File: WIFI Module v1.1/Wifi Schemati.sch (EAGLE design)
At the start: 25 parts, among them IC1 PIC24FVXXKA302-SP

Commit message: Moving Around Board
- Rotated ESP 180, fixed reprog issue
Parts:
- added SHORT_TO_RST: (no value), pinhead:PINHD-1X1
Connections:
- removed net N$3: R3.2, U$1.GPIO2
- new net N$12: R4.1, R5.1
- net 3.3V: no longer R4.1, R5.2
- net CLK: now also R3.2
- net FLSH_MD: no longer R4.2
- net MOSI: now also R4.2
- net N$1: now also SHORT_TO_RST.1; no longer R5.1
- net SS: now also R5.2

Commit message: v1.1 PCB Changes
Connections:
- removed net N$12: R4.1, R5.1
- net 3.3V: no longer R3.1
- net VDD: now also R3.1, R4.1, R5.1
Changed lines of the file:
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@@
 <?xml version="1.0" encoding="utf-8"?>
 <!DOCTYPE eagle SYSTEM "eagle.dtd">
-<eagle version="9.2.2">
+<eagle version="9.3.0">
 <drawing>
 <settings>
@@
 <label x="0" y="88.9" size="1.778" layer="95"/>
 </segment>
+<segment>
+<pinref part="R5" gate="G$1" pin="1"/>
+<wire x1="25.4" y1="25.4" x2="27.94" y2="25.4" width="0.1524" layer="91"/>
+<wire x1="27.94" y1="22.86" x2="27.94" y2="25.4" width="0.1524" layer="91"/>
+<pinref part="R3" gate="G$1" pin="1"/>
+<wire x1="25.4" y1="22.86" x2="27.94" y2="22.86" width="0.1524" layer="91"/>
+<label x="27.94" y="22.86" size="1.778" layer="95"/>
+<pinref part="R4" gate="G$1" pin="1"/>
+<wire x1="25.4" y1="20.32" x2="27.94" y2="20.32" width="0.1524" layer="91"/>
+<wire x1="27.94" y1="20.32" x2="27.94" y2="22.86" width="0.1524" layer="91"/>
+<junction x="27.94" y="22.86"/>
+</segment>
 </net>
 <net name="SPI_LIGHT" class="0">
@@
 <wire x1="243.84" y1="20.32" x2="238.76" y2="20.32" width="0.1524" layer="91"/>
 </segment>
-<segment>
-<pinref part="R3" gate="G$1" pin="1"/>
-<wire x1="25.4" y1="22.86" x2="30.48" y2="22.86" width="0.1524" layer="91"/>
-<label x="30.48" y="22.86" size="1.778" layer="95"/>
-</segment>
 </net>
 <net name="N$2" class="0">
@@
 </segment>
 </net>
-<net name="N$12" class="0">
-<segment>
-<pinref part="R5" gate="G$1" pin="1"/>
-<wire x1="25.4" y1="25.4" x2="27.94" y2="25.4" width="0.1524" layer="91"/>
-<pinref part="R4" gate="G$1" pin="1"/>
-<wire x1="25.4" y1="20.32" x2="27.94" y2="20.32" width="0.1524" layer="91"/>
-<wire x1="27.94" y1="20.32" x2="27.94" y2="25.4" width="0.1524" layer="91"/>
-</segment>
-</net>

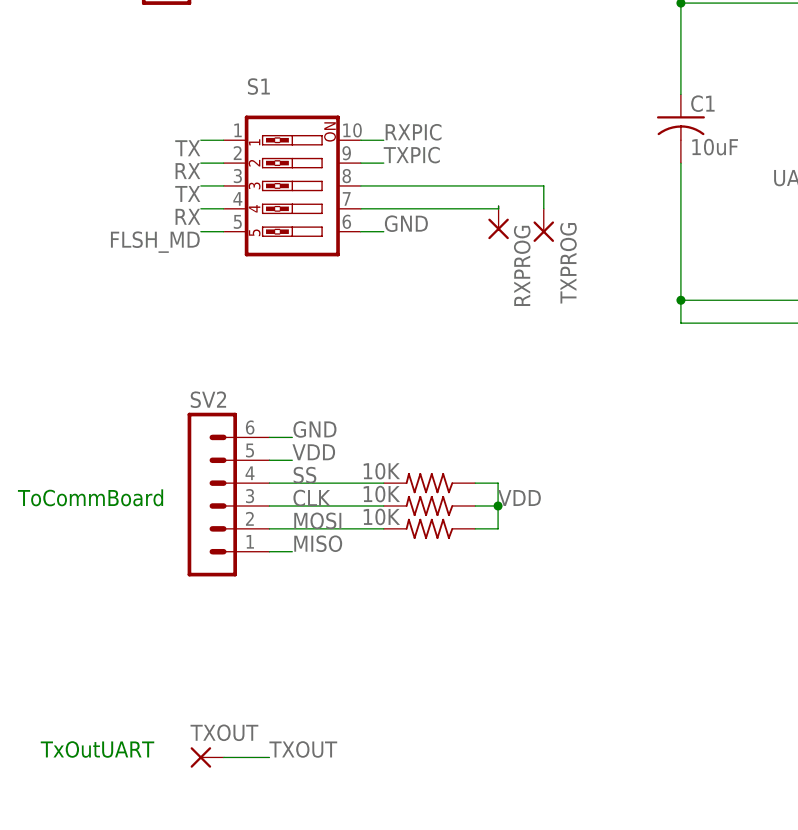
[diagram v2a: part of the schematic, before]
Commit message: Update PCB, 3V3.lbr, and grbs
Made edits to PCB after milling v1.1
Updated 3v3.lbr footprint
Added gerbers from latest mill
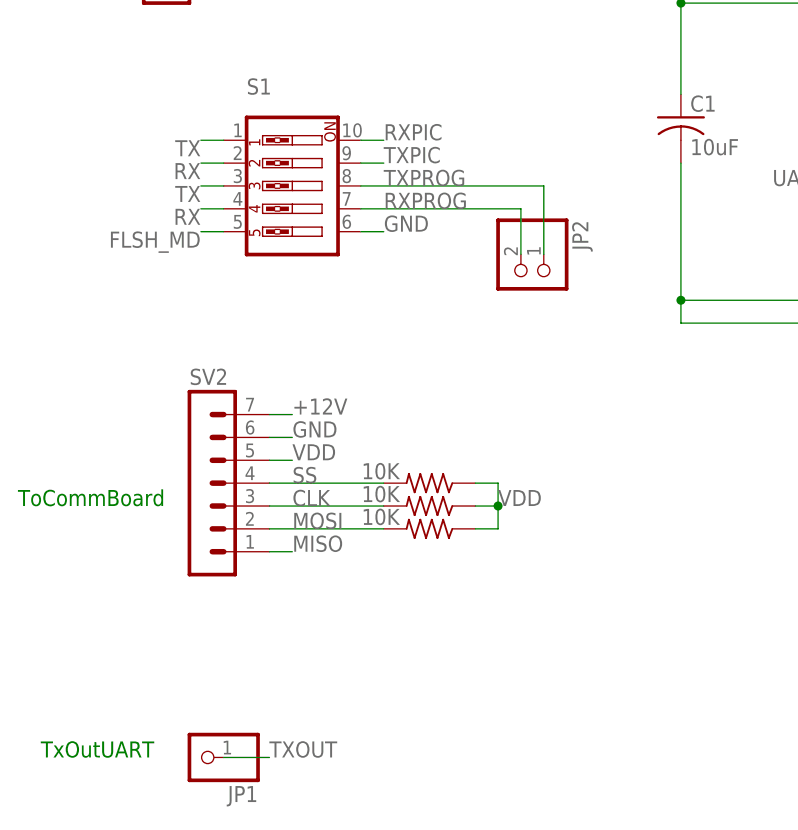
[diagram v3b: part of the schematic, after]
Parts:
- removed RXPROG, TXOUT, TXPROG: (no value), wirepad:1,6/0,8
- added JP1: (no value), pinhead:PINHD-1X1
- added JP2: (no value), pinhead:PINHD-1X2
- SV2: device con-lstb:MA06-1 -> con-lstb:MA07-1
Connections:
- removed net N$4: S1.8, TXPROG.P
- removed net N$5: RXPROG.P, S1.7
- new net +12V: SV2.7
- new net RXPROG: JP2.2, S1.7
- new net TXPROG: JP2.1, S1.8
- net TXOUT: now also JP1.1; no longer TXOUT.P
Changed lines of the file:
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@@
 <?xml version="1.0" encoding="utf-8"?>
 <!DOCTYPE eagle SYSTEM "eagle.dtd">
-<eagle version="9.3.0">
+<eagle version="9.2.2">
 <drawing>
 <settings>
@@
 <part name="WIFI" library="led" library_urn="urn:adsk.eagle:library:259" deviceset="U57X32" device="" package3d_urn="urn:adsk.eagle:package:15789/1"/>
 <part name="C2" library="rcl" library_urn="urn:adsk.eagle:library:334" deviceset="C-US" device="025-025X050" package3d_urn="urn:adsk.eagle:package:23629/2" value="10uF"/>
-<part name="TXOUT" library="wirepad" library_urn="urn:adsk.eagle:library:412" deviceset="1,6/0,8" device="" package3d_urn="urn:adsk.eagle:package:30830/1"/>
 <part name="S1" library="special" library_urn="urn:adsk.eagle:library:367" deviceset="SW_DIP-5" device="" package3d_urn="urn:adsk.eagle:package:26656/2"/>
 <part name="R2" library="rcl" library_urn="urn:adsk.eagle:library:334" deviceset="R-US_" device="0207/7" package3d_urn="urn:adsk.eagle:package:23493/2" value="10K"/>
-<part name="TXPROG" library="wirepad" library_urn="urn:adsk.eagle:library:412" deviceset="1,6/0,8" device="" package3d_urn="urn:adsk.eagle:package:30830/1"/>
-<part name="RXPROG" library="wirepad" library_urn="urn:adsk.eagle:library:412" deviceset="1,6/0,8" device="" package3d_urn="urn:adsk.eagle:package:30830/1"/>
 <part name="R6" library="rcl" library_urn="urn:adsk.eagle:library:334" deviceset="R-US_" device="0207/7" package3d_urn="urn:adsk.eagle:package:23493/2" value="10K"/>
 <part name="CR1" library="3v3 Regulator" deviceset="LD1117V33" device=""/>
 <part name="SV1" library="con-lstb" library_urn="urn:adsk.eagle:library:162" deviceset="MA05-1" device="" package3d_urn="urn:adsk.eagle:package:8332/1"/>
-<part name="SV2" library="con-lstb" library_urn="urn:adsk.eagle:library:162" deviceset="MA06-1" device="" package3d_urn="urn:adsk.eagle:package:8340/1"/>
 <part name="R3" library="rcl" library_urn="urn:adsk.eagle:library:334" deviceset="R-US_" device="0207/7" package3d_urn="urn:adsk.eagle:package:23493/2" value="10K"/>
 <part name="R4" library="rcl" library_urn="urn:adsk.eagle:library:334" deviceset="R-US_" device="0207/7" package3d_urn="urn:adsk.eagle:package:23493/2" value="10K"/>
 <part name="R5" library="rcl" library_urn="urn:adsk.eagle:library:334" deviceset="R-US_" device="0207/7" package3d_urn="urn:adsk.eagle:package:23493/2" value="10K"/>
 <part name="SHORT_TO_RST" library="pinhead" library_urn="urn:adsk.eagle:library:325" deviceset="PINHD-1X1" device="" package3d_urn="urn:adsk.eagle:package:22485/2"/>
+<part name="SV2" library="con-lstb" library_urn="urn:adsk.eagle:library:162" deviceset="MA07-1" device="" package3d_urn="urn:adsk.eagle:package:8341/1"/>
+<part name="JP1" library="pinhead" library_urn="urn:adsk.eagle:library:325" deviceset="PINHD-1X1" device="" package3d_urn="urn:adsk.eagle:package:22485/2"/>
+<part name="JP2" library="pinhead" library_urn="urn:adsk.eagle:library:325" deviceset="PINHD-1X2" device="" package3d_urn="urn:adsk.eagle:package:22435/2"/>
 </parts>
 <sheets>
@@
 <attribute name="VALUE" x="252.984" y="24.511" size="1.778" layer="96" rot="R180"/>
 </instance>
-<instance part="TXOUT" gate="P" x="-5.08" y="-5.08" smashed="yes">
-<attribute name="NAME" x="-6.223" y="-3.2258" size="1.778" layer="95"/>
-<attribute name="VALUE" x="-6.223" y="-8.382" size="1.778" layer="96"/>
-</instance>
 <instance part="S1" gate="A" x="5.08" y="58.42" smashed="yes" rot="R180">
 <attribute name="NAME" x="0" y="68.58" size="1.778" layer="95"/>
@@
 <attribute name="VALUE" x="256.61" y="74.098" size="1.778" layer="96"/>
 </instance>
-<instance part="TXPROG" gate="P" x="33.02" y="53.34" smashed="yes" rot="R90">
-<attribute name="NAME" x="34.8742" y="54.483" size="1.778" layer="95" rot="R270"/>
-<attribute name="VALUE" x="36.322" y="52.197" size="1.778" layer="96" rot="R90"/>
-</instance>
-<instance part="RXPROG" gate="P" x="27.99925" y="53.649809375" smashed="yes" rot="R90">
-<attribute name="NAME" x="29.73495" y="54.173190625" size="1.778" layer="95" rot="R270"/>
-<attribute name="VALUE" x="31.30125" y="52.506809375" size="1.778" layer="96" rot="R90"/>
-</instance>
 <instance part="R6" gate="G$1" x="220.98" y="83.82" smashed="yes" rot="R180">
 <attribute name="VALUE" x="224.79" y="87.122" size="1.778" layer="96" rot="R180"/>
@@
 <attribute name="NAME" x="-11.43" y="94.742" size="1.778" layer="95"/>
 </instance>
-<instance part="SV2" gate="1" x="-5.08" y="25.4" smashed="yes">
-<attribute name="VALUE" x="-6.35" y="12.7" size="1.778" layer="96"/>
-<attribute name="NAME" x="-6.35" y="33.782" size="1.778" layer="95"/>
-</instance>
 <instance part="R3" gate="G$1" x="20.32" y="22.86" smashed="yes" rot="R180">
 <attribute name="VALUE" x="12.77" y="23.298" size="1.778" layer="96"/>
@@
 <attribute name="NAME" x="209.55" y="88.265" size="1.778" layer="95" rot="R180"/>
 <attribute name="VALUE" x="209.55" y="96.52" size="1.778" layer="96" rot="R180"/>
+</instance>
+<instance part="SV2" gate="1" x="-5.08" y="25.4" smashed="yes">
+<attribute name="VALUE" x="-6.35" y="12.7" size="1.778" layer="96"/>
+<attribute name="NAME" x="-6.35" y="36.322" size="1.778" layer="95"/>
+</instance>
+<instance part="JP1" gate="G$1" x="-5.08" y="-5.08" smashed="yes" rot="R180">
+<attribute name="NAME" x="1.27" y="-8.255" size="1.778" layer="95" rot="R180"/>
+<attribute name="VALUE" x="1.27" y="0" size="1.778" layer="96" rot="R180"/>
+</instance>
+<instance part="JP2" gate="G$1" x="30.48" y="48.26" smashed="yes" rot="R270">
+<attribute name="NAME" x="36.195" y="54.61" size="1.778" layer="95" rot="R270"/>
+<attribute name="VALUE" x="25.4" y="54.61" size="1.778" layer="96" rot="R270"/>
 </instance>
 </instances>
@@
 </segment>
 <segment>
-<pinref part="SV2" gate="1" pin="6"/>
 <wire x1="2.54" y1="30.48" x2="5.08" y2="30.48" width="0.1524" layer="91"/>
 <label x="5.08" y="30.48" size="1.778" layer="95"/>
+<pinref part="SV2" gate="1" pin="6"/>
 </segment>
 <segment>
@@
 </segment>
 <segment>
-<pinref part="SV2" gate="1" pin="5"/>
 <wire x1="2.54" y1="27.94" x2="5.08" y2="27.94" width="0.1524" layer="91"/>
 <label x="5.08" y="27.94" size="1.778" layer="95"/>
+<pinref part="SV2" gate="1" pin="5"/>
 </segment>
 <segment>
@@
 </segment>
 <segment>
-<pinref part="SV2" gate="1" pin="1"/>
 <wire x1="2.54" y1="17.78" x2="5.08" y2="17.78" width="0.1524" layer="91"/>
 <label x="5.08" y="17.78" size="1.778" layer="95"/>
+<pinref part="SV2" gate="1" pin="1"/>
 </segment>
 </net>
@@
 </segment>
 <segment>
-<pinref part="SV2" gate="1" pin="2"/>
 <label x="5.08" y="20.32" size="1.778" layer="95"/>
 <pinref part="R4" gate="G$1" pin="2"/>
 <wire x1="2.54" y1="20.32" x2="15.24" y2="20.32" width="0.1524" layer="91"/>
+<pinref part="SV2" gate="1" pin="2"/>
 </segment>
 </net>
@@
 </segment>
 <segment>
-<pinref part="SV2" gate="1" pin="3"/>
 <label x="5.08" y="22.86" size="1.778" layer="95"/>
 <pinref part="R3" gate="G$1" pin="2"/>
 <wire x1="2.54" y1="22.86" x2="15.24" y2="22.86" width="0.1524" layer="91"/>
+<pinref part="SV2" gate="1" pin="3"/>
 </segment>
 </net>
@@
 </segment>
 <segment>
-<pinref part="SV2" gate="1" pin="4"/>
 <label x="5.08" y="25.4" size="1.778" layer="95"/>
 <pinref part="R5" gate="G$1" pin="2"/>
 <wire x1="2.54" y1="25.4" x2="15.24" y2="25.4" width="0.1524" layer="91"/>
+<pinref part="SV2" gate="1" pin="4"/>
 </segment>
 </net>
@@
 </segment>
 </net>
-<net name="N$4" class="0">
+<net name="TXPROG" class="0">
 <segment>
 <pinref part="S1" gate="A" pin="8"/>
 <wire x1="12.7" y1="58.42" x2="33.02" y2="58.42" width="0.1524" layer="91"/>
-<pinref part="TXPROG" gate="P" pin="P"/>
-<wire x1="33.02" y1="58.42" x2="33.02" y2="55.88" width="0.1524" layer="91"/>
-</segment>
-</net>
-<net name="N$5" class="0">
+<pinref part="JP2" gate="G$1" pin="1"/>
+<wire x1="33.02" y1="58.42" x2="33.02" y2="50.8" width="0.1524" layer="91"/>
+<label x="15.24" y="58.42" size="1.778" layer="95"/>
+</segment>
+</net>
+<net name="RXPROG" class="0">
 <segment>
 <pinref part="S1" gate="A" pin="7"/>
-<pinref part="RXPROG" gate="P" pin="P"/>
-<wire x1="12.7" y1="55.88" x2="27.99925" y2="55.88" width="0.1524" layer="91"/>
-<wire x1="27.99925" y1="55.88" x2="27.99925" y2="56.189809375" width="0.1524" layer="91"/>
+<wire x1="12.7" y1="55.88" x2="30.48" y2="55.88" width="0.1524" layer="91"/>
+<pinref part="JP2" gate="G$1" pin="2"/>
+<wire x1="30.48" y1="55.88" x2="30.48" y2="50.8" width="0.1524" layer="91"/>
+<label x="15.24" y="55.88" size="1.778" layer="95"/>
 </segment>
 </net>
@@
 </segment>
 <segment>
-<pinref part="TXOUT" gate="P" pin="P"/>
 <wire x1="-2.54" y1="-5.08" x2="2.54" y2="-5.08" width="0.1524" layer="91"/>
 <label x="2.54" y="-5.08" size="1.778" layer="95"/>
+<pinref part="JP1" gate="G$1" pin="1"/>
 </segment>
 </net>
@@
 </segment>
 </net>
+<net name="+12V" class="0">
+<segment>
+<pinref part="SV2" gate="1" pin="7"/>
+<wire x1="2.54" y1="33.02" x2="5.08" y2="33.02" width="0.1524" layer="91"/>
+<label x="5.08" y="33.02" size="1.778" layer="95"/>
+</segment>
+</net>

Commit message: ITS ALIVE
Currently (Hardware) Working, smaller board. Rev. 1.1
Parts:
- renumbered CR1 to LD33V3, JP1 to URT_OUT, JP2 to ESP_FIRMWARE, S1 to DIP, SHORT_TO_RST to RST_SHORT, SV1 to PICKIT, SV2 to TO_CB, U$1 to HUG_TOM
